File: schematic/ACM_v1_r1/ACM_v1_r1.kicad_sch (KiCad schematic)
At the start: 26 parts, among them J1 DF40C-60DS-0.4V(51), J2 DF40C-60DS-0.4V(51), J4 Conn_01x02, SW1 RST

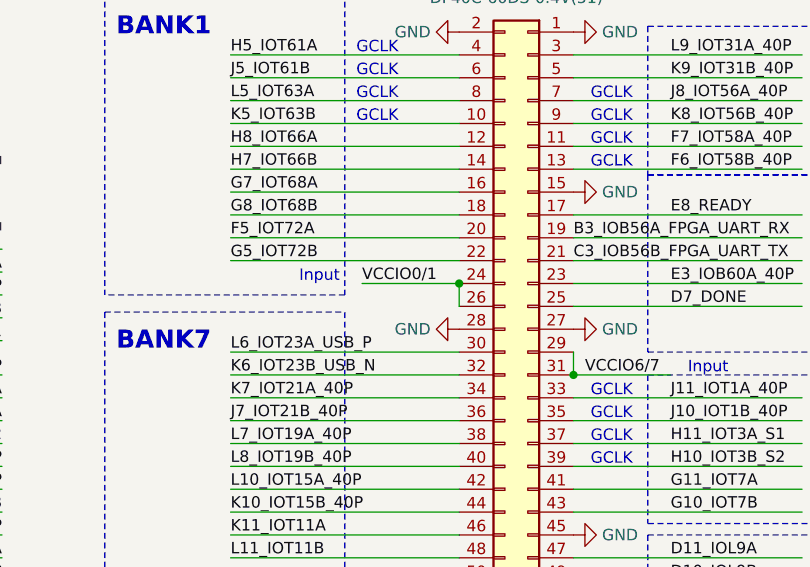
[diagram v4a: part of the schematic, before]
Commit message: seems like everything is routed? off by 1 error for I2C FPGA pins fixed?
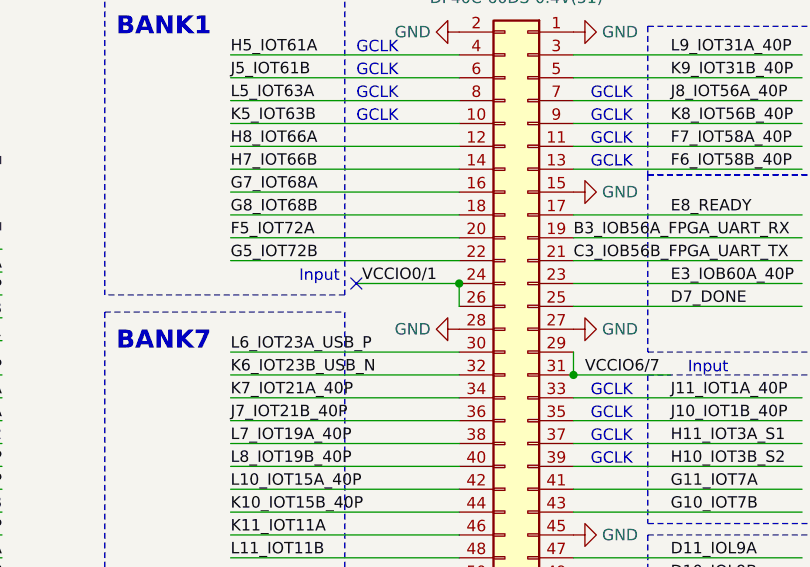
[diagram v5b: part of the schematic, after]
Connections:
- no-connect marks 11 -> 12
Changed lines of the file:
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@@
+	)
+	(junction
+		(at 224.155 96.52)
+		(diameter 0)
+		(color 0 0 0 0)
+	)
+	(junction
+		(at 224.155 93.98)
+		(diameter 0)
+		(color 0 0 0 0)
+	)
+	(junction
+		(at 224.155 101.6)
+		(diameter 0)
+		(color 0 0 0 0)
+	)
+	(junction
+		(at 119.38 173.99)
+		(diameter 0)
+		(color 0 0 0 0)
+	)
+	(junction
+		(at 224.155 83.82)
+		(diameter 0)
+		(color 0 0 0 0)
+	)
+	(junction
+		(at 15.24 177.8)
+		(diameter 0)
+		(color 0 0 0 0)
+	)
+	(junction
+		(at 41.91 177.8)
+		(diameter 0)
+		(color 0 0 0 0)
+	)
+	(junction
+		(at 224.155 27.94)
+		(diameter 0)
+		(color 0 0 0 0)
 	)
 	(junction
@@
 	)
 	(junction
-		(at 224.155 96.52)
-		(diameter 0)
-		(color 0 0 0 0)
-	)
-	(junction
-		(at 224.155 93.98)
-		(diameter 0)
-		(color 0 0 0 0)
-	)
-	(junction
-		(at 224.155 101.6)
-		(diameter 0)
-		(color 0 0 0 0)
-	)
-	(junction
-		(at 119.38 173.99)
-		(diameter 0)
-		(color 0 0 0 0)
-	)
-	(junction
-		(at 224.155 83.82)
-		(diameter 0)
-		(color 0 0 0 0)
-	)
-	(junction
-		(at 15.24 177.8)
-		(diameter 0)
-		(color 0 0 0 0)
-	)
-	(junction
-		(at 41.91 177.8)
-		(diameter 0)
-		(color 0 0 0 0)
-	)
-	(junction
-		(at 224.155 27.94)
-		(diameter 0)
-		(color 0 0 0 0)
-	)
-	(junction
 		(at 224.155 86.36)
 		(diameter 0)
@@
 	)
 	(no_connect
+		(at 125.73 55.88)
+	)
+	(no_connect
 		(at 265.43 76.2)
 	)
@@
 	(wire
 		(pts
-			(xy 126.365 55.88) (xy 137.16 55.88)
-		)
-		(stroke
+			(xy 125.73 55.88) (xy 137.16 55.88)
+		)
+		(stroke

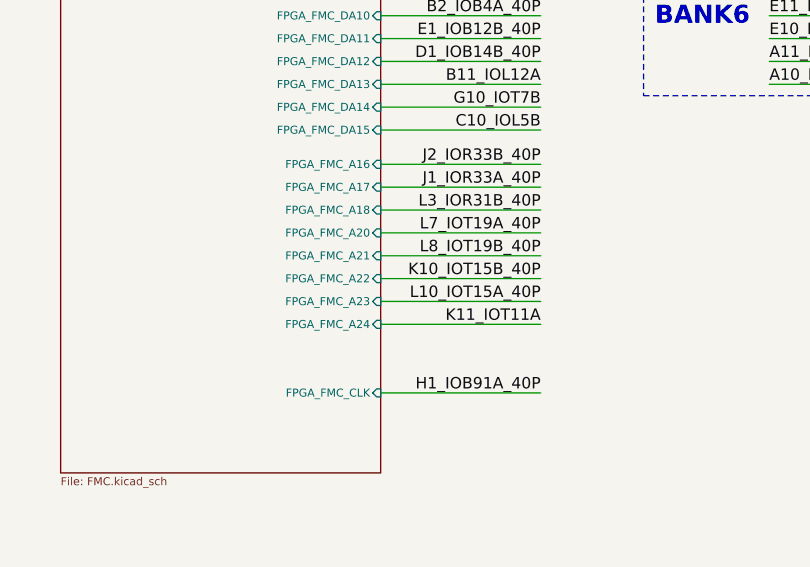
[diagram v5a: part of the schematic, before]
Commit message: adding renders and render script
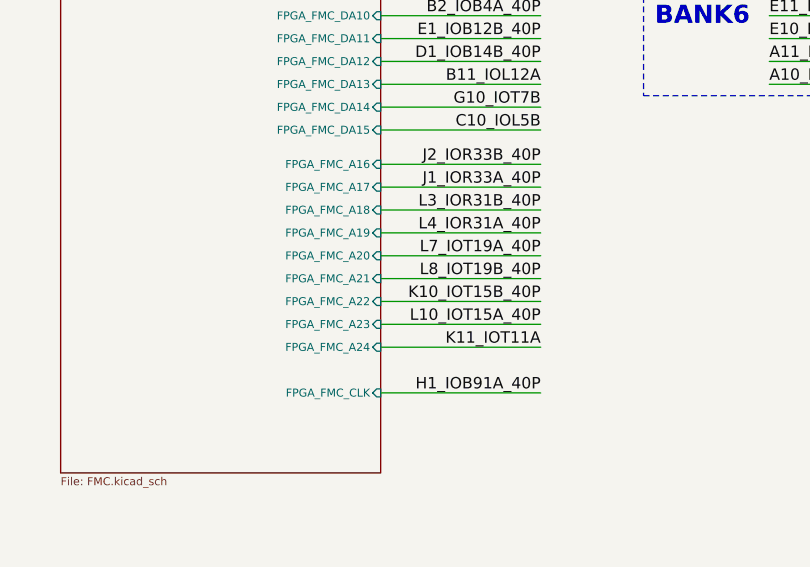
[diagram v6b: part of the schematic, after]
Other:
- sheet FMC ports: added FPGA_FMC_A19; removed none
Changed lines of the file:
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@@
 	(wire
 		(pts
-			(xy 86.36 115.57) (xy 68.58 115.57)
+			(xy 86.36 118.11) (xy 68.58 118.11)
 		)
 		(stroke
@@
 	(wire
 		(pts
-			(xy 86.36 125.73) (xy 68.58 125.73)
+			(xy 86.36 128.27) (xy 68.58 128.27)
 		)
 		(stroke
@@
 	(wire
 		(pts
-			(xy 86.36 118.11) (xy 68.58 118.11)
+			(xy 86.36 120.65) (xy 68.58 120.65)
 		)
 		(stroke
@@
 	(wire
 		(pts
-			(xy 86.36 123.19) (xy 68.58 123.19)
+			(xy 86.36 125.73) (xy 68.58 125.73)
 		)
 		(stroke
@@
 	(wire
 		(pts
+			(xy 86.36 115.57) (xy 68.58 115.57)
+		)
+		(stroke
+			(width 0)
+			(type default)
+		)
+	)
+	(wire
+		(pts
 			(xy 86.36 133.35) (xy 68.58 133.35)
 		)
@@
 	(wire
 		(pts
-			(xy 86.36 120.65) (xy 68.58 120.65)
+			(xy 86.36 123.19) (xy 68.58 123.19)
 		)
 		(stroke
@@
 	)
 	(label "K11_IOT11A"
-		(at 86.36 125.73 180)
+		(at 86.36 128.27 180)
 		(effects
 			(font
@@
 	)
 	(label "K10_IOT15B_40P"
-		(at 86.36 120.65 180)
+		(at 86.36 123.19 180)
 		(effects
 			(font
@@
 	)
 	(label "L8_IOT19B_40P"
-		(at 86.36 118.11 180)
+		(at 86.36 120.65 180)
 		(effects
 			(font
@@
 	)
 	(label "L7_IOT19A_40P"
-		(at 86.36 115.57 180)
+		(at 86.36 118.11 180)
 		(effects
 			(font
@@
 	)
 	(label "L10_IOT15A_40P"
-		(at 86.36 123.19 180)
+		(at 86.36 125.73 180)
 		(effects
 			(font
@@
 		)
 	)
+	(label "L4_IOR31A_40P"
+		(at 86.36 115.57 180)
+		(effects
+			(font
+				(size 1.27 1.27)
+			)
+			(justify right bottom)
+		)
+	)
 	(label "H7_IOT66B"
 		(at 111.76 43.18 0)
@@
 		)
 		(pin "FPGA_FMC_A20" input
-			(at 68.58 115.57 0)
+			(at 68.58 118.11 0)
 			(effects
 				(font
@@
 		)
 		(pin "FPGA_FMC_A21" input
-			(at 68.58 118.11 0)
+			(at 68.58 120.65 0)
 			(effects
 				(font
@@
 		)
 		(pin "FPGA_FMC_A22" input
-			(at 68.58 120.65 0)
+			(at 68.58 123.19 0)
 			(effects
 				(font
@@
 		)
 		(pin "FPGA_FMC_A23" input
-			(at 68.58 123.19 0)
+			(at 68.58 125.73 0)
 			(effects
 				(font
@@
 		)
 		(pin "FPGA_FMC_A24" input
-			(at 68.58 125.73 0)
+			(at 68.58 128.27 0)
 			(effects
 				(font
@@
 			(effects
 				(font
+					(size 0.889 0.889)
+				)
+				(justify right)
+			)
+		)
+		(pin "FPGA_FMC_A19" input
+			(at 68.58 115.57 0)
+			(effects
+				(font
